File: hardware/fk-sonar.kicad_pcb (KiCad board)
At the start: 2 copper layers, 34.5 x 70.4 mm, 81 parts, among them J1 CONN_01x03, J10 CONN_01x02, J2 CONN_02x05_SWD, J3 RF-SMA-EDGE, J4 MICRO-USB, J5 S2B-PH-SM4-TB, J6 CONN_01x04, J7 S2B-PH-SM4-TB, J8 CONN_01x03_SERIAL, J9 CONN_01x05, M1 MOUNT_HOLE, M3 MOUNT_HOLE, M4 MOUNT_HOLE, M6 MOUNT_HOLE, Q1 2N7002LT1G, SW1 SPNO, U1 ATSAMD21G18A-AU, U2 RFM95W, U3 BQ24074RGTT, U4 S25FL116K0XMFI041, U5 MAX1704XX, U6 MCP1700T-3302E/MB, U7 SK6812, U8 TPS2051B, Y1 FC-135

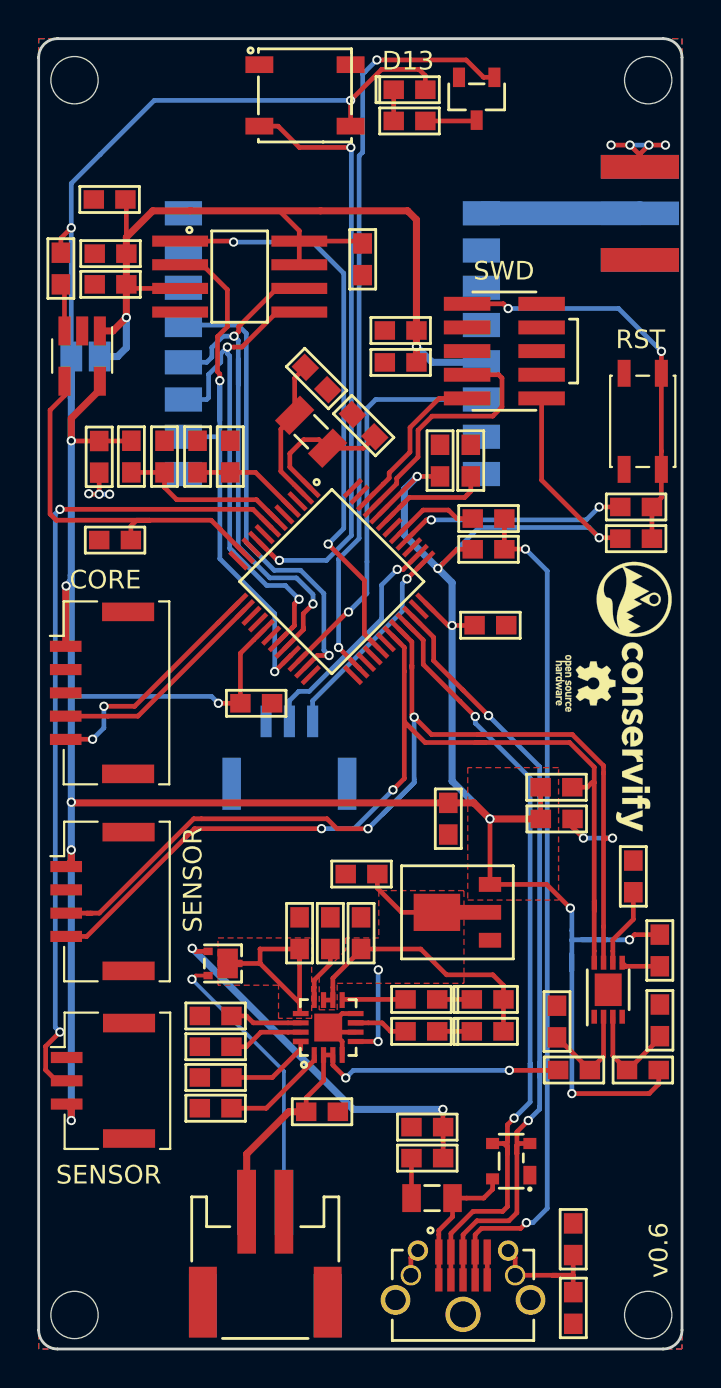
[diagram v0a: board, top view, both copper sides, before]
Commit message: Switch to 2.7mm mounting holes.
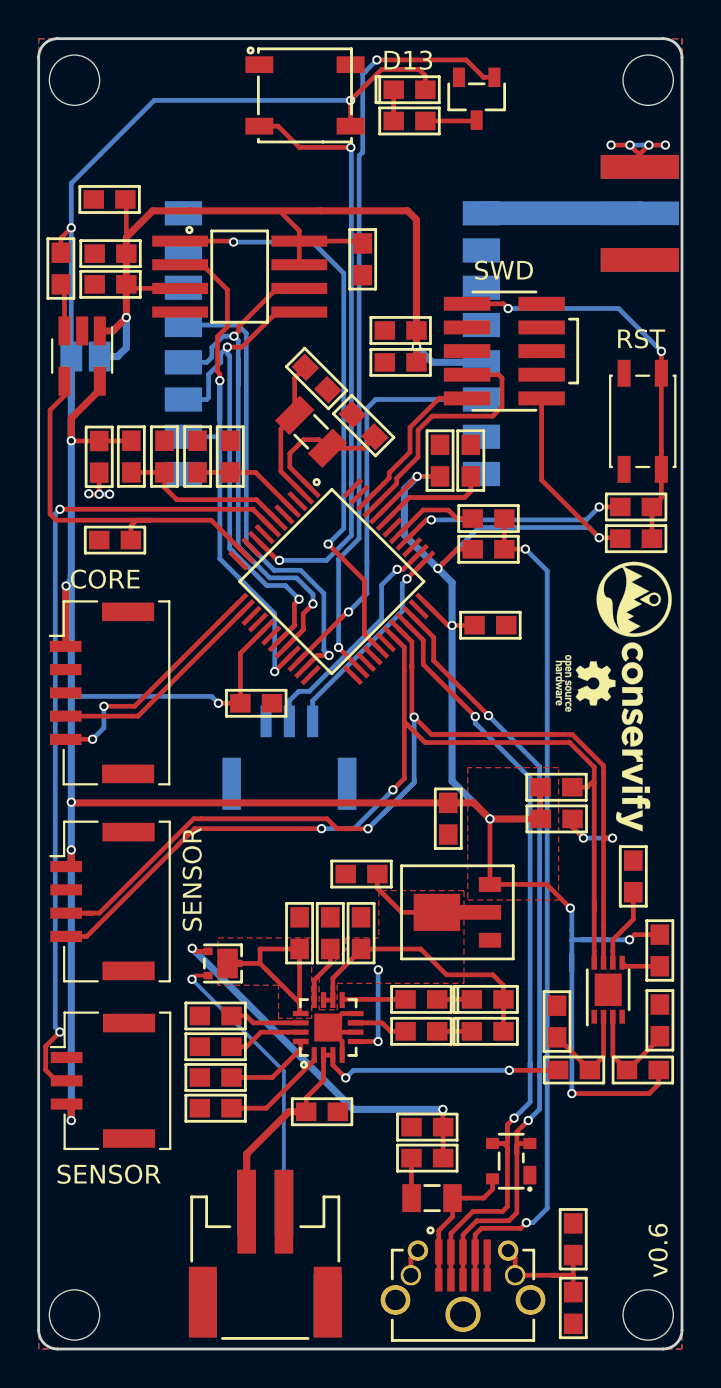
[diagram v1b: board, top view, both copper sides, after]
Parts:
- M1, M3, M4, M6: footprint conservify:HOLE_NPTH_2.54MM -> conservify:HOLE_NPTH_2.7MM
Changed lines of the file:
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@@
     )
-  )
-  (module conservify:HOLE_NPTH_2.54MM (layer F.Cu)
-    (at 154.9028 64.4608)
-    (fp_text reference M1 (at 0 -2.54) (layer F.SilkS) hide
-      (effects (font (size 1 1) (thickness 0.15)))
-    )
-    (fp_text value MOUNT_HOLE (at 0 2.54) (layer F.Fab)
-      (effects (font (size 1 1) (thickness 0.15)))
-    )
-    (pad "" np_thru_hole circle (at 0 0) (size 2.54 2.54) (drill 2.54) (layers *.Cu *.Mask F.SilkS))
-  )
-  (module conservify:HOLE_NPTH_2.54MM (layer F.Cu)
-    (at 124.1 130.7608)
-    (fp_text reference M3 (at 0 -2.54) (layer F.SilkS) hide
-      (effects (font (size 1 1) (thickness 0.15)))
-    )
-    (fp_text value MOUNT_HOLE (at 0 2.54) (layer F.Fab)
-      (effects (font (size 1 1) (thickness 0.15)))
-    )
-    (pad "" np_thru_hole circle (at 0 0) (size 2.54 2.54) (drill 2.54) (layers *.Cu *.Mask F.SilkS))
-  )
-  (module conservify:HOLE_NPTH_2.54MM (layer F.Cu)
-    (at 154.9028 130.7608)
-    (fp_text reference M4 (at 0 -2.54) (layer F.SilkS) hide
-      (effects (font (size 1 1) (thickness 0.15)))
-    )
-    (fp_text value MOUNT_HOLE (at 0 2.54) (layer F.Fab)
-      (effects (font (size 1 1) (thickness 0.15)))
-    )
-    (pad "" np_thru_hole circle (at 0 0) (size 2.54 2.54) (drill 2.54) (layers *.Cu *.Mask F.SilkS))
-  )
-  (module conservify:HOLE_NPTH_2.54MM (layer F.Cu)
-    (at 124.1 64.4608)
-    (fp_text reference M6 (at 0 -2.54) (layer F.SilkS) hide
-      (effects (font (size 1 1) (thickness 0.15)))
-    )
-    (fp_text value MOUNT_HOLE (at 0 2.54) (layer F.Fab)
-      (effects (font (size 1 1) (thickness 0.15)))
-    )
-    (pad "" np_thru_hole circle (at 0 0) (size 2.54 2.54) (drill 2.54) (layers *.Cu *.Mask F.SilkS))
   )
   (module conservify:RES-0603 (layer F.Cu)
@@
     (pad 2 smd rect (at 0.85 0) (size 1.1 1) (layers F.Cu F.Paste F.Mask)
       (net 86 /PERIPH_3V3))
+  )
+  (module conservify:HOLE_NPTH_2.7MM (layer F.Cu)
+    (at 154.9028 64.4608)
+    (fp_text reference M1 (at 0 -2.54) (layer F.SilkS) hide
+      (effects (font (size 1 1) (thickness 0.15)))
+    )
+    (fp_text value MOUNT_HOLE (at 0 2.54) (layer F.Fab)
+      (effects (font (size 1 1) (thickness 0.15)))
+    )
+    (pad "" np_thru_hole circle (at 0 0) (size 2.7 2.7) (drill 2.7) (layers *.Cu *.Mask F.SilkS))
+  )
+  (module conservify:HOLE_NPTH_2.7MM (layer F.Cu)
+    (at 124.1 130.7608)
+    (fp_text reference M3 (at 0 -2.54) (layer F.SilkS) hide
+      (effects (font (size 1 1) (thickness 0.15)))
+    )
+    (fp_text value MOUNT_HOLE (at 0 2.54) (layer F.Fab)
+      (effects (font (size 1 1) (thickness 0.15)))
+    )
+    (pad "" np_thru_hole circle (at 0 0) (size 2.7 2.7) (drill 2.7) (layers *.Cu *.Mask F.SilkS))
+  )
+  (module conservify:HOLE_NPTH_2.7MM (layer F.Cu)
+    (at 154.9028 130.7608)
+    (fp_text reference M4 (at 0 -2.54) (layer F.SilkS) hide
+      (effects (font (size 1 1) (thickness 0.15)))
+    )
+    (fp_text value MOUNT_HOLE (at 0 2.54) (layer F.Fab)
+      (effects (font (size 1 1) (thickness 0.15)))
+    )
+    (pad "" np_thru_hole circle (at 0 0) (size 2.7 2.7) (drill 2.7) (layers *.Cu *.Mask F.SilkS))
+  )
+  (module conservify:HOLE_NPTH_2.7MM (layer F.Cu)
+    (at 124.1 64.4608)
+    (fp_text reference M6 (at 0 -2.54) (layer F.SilkS) hide
+      (effects (font (size 1 1) (thickness 0.15)))
+    )
+    (fp_text value MOUNT_HOLE (at 0 2.54) (layer F.Fab)
+      (effects (font (size 1 1) (thickness 0.15)))
+    )
+    (pad "" np_thru_hole circle (at 0 0) (size 2.7 2.7) (drill 2.7) (layers *.Cu *.Mask F.SilkS))
   )
   (gr_text DEBUG (at 135.8392 105.5878 180) (layer B.SilkS)
@@
     (connect_pads (clearance 0.2032))
     (min_thickness 0.2032)
-    (fill yes (arc_segments 32) (thermal_gap 0.254) (thermal_bridge_width 0.254))
+    (fill (arc_segments 32) (thermal_gap 0.254) (thermal_bridge_width 0.254))
     (polygon
       (pts
@@
     (connect_pads (clearance 0.2032))
     (min_thickness 0.2032)
-    (fill yes (arc_segments 16) (thermal_gap 0.254) (thermal_bridge_width 0.254))
+    (fill (arc_segments 16) (thermal_gap 0.254) (thermal_bridge_width 0.254))
     (polygon
       (pts
@@
     (connect_pads (clearance 0.2032))
     (min_thickness 0.2032)
-    (fill yes (arc_segments 32) (thermal_gap 0.254) (thermal_bridge_width 0.254))
+    (fill (arc_segments 32) (thermal_gap 0.254) (thermal_bridge_width 0.254))
     (polygon
       (pts
@@
     (connect_pads (clearance 0.2032))
     (min_thickness 0.2032)
-    (fill yes (arc_segments 32) (thermal_gap 0.254) (thermal_bridge_width 0.254))
+    (fill (arc_segments 32) (thermal_gap 0.254) (thermal_bridge_width 0.254))
     (polygon
       (pts
@@
     (connect_pads (clearance 0.2032))
     (min_thickness 0.2032)
-    (fill yes (arc_segments 32) (thermal_gap 0.254) (thermal_bridge_width 0.254))
+    (fill (arc_segments 32) (thermal_gap 0.254) (thermal_bridge_width 0.254))
     (polygon
       (pts

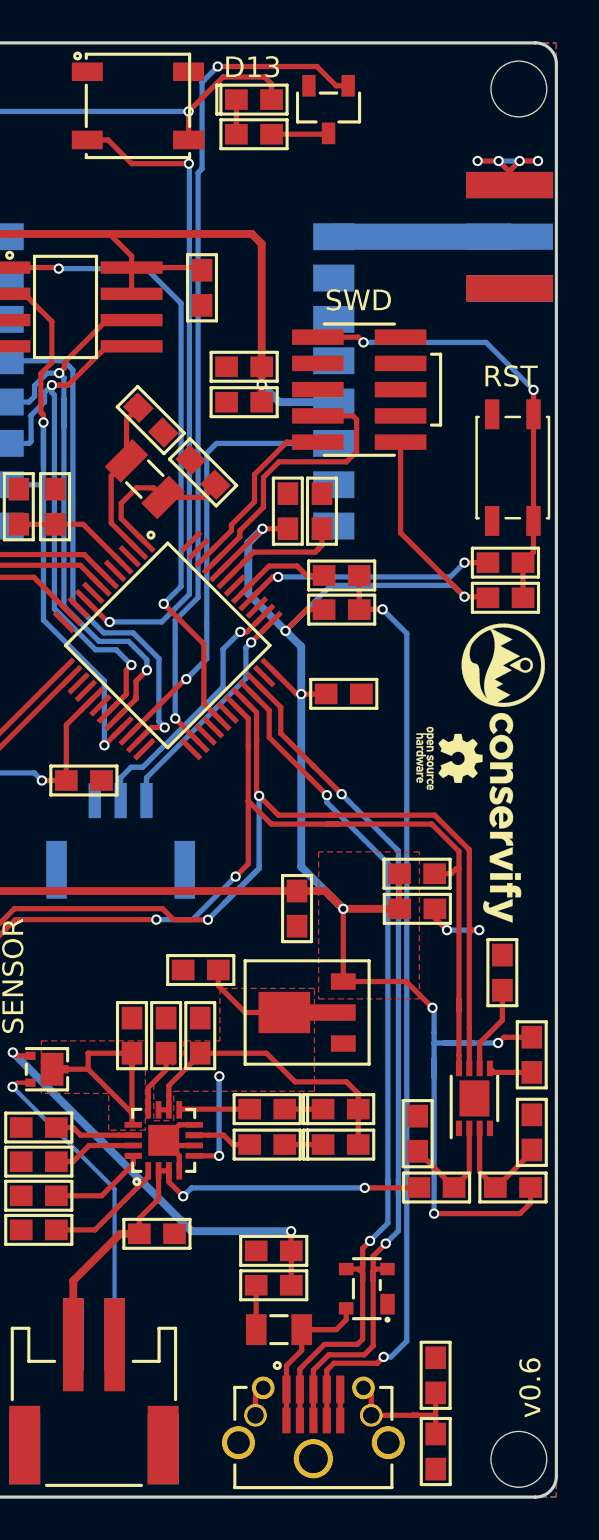
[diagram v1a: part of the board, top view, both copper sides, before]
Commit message: Deleted charging, LoRa, fuel gauge, swapped out connectors and peripheral switch
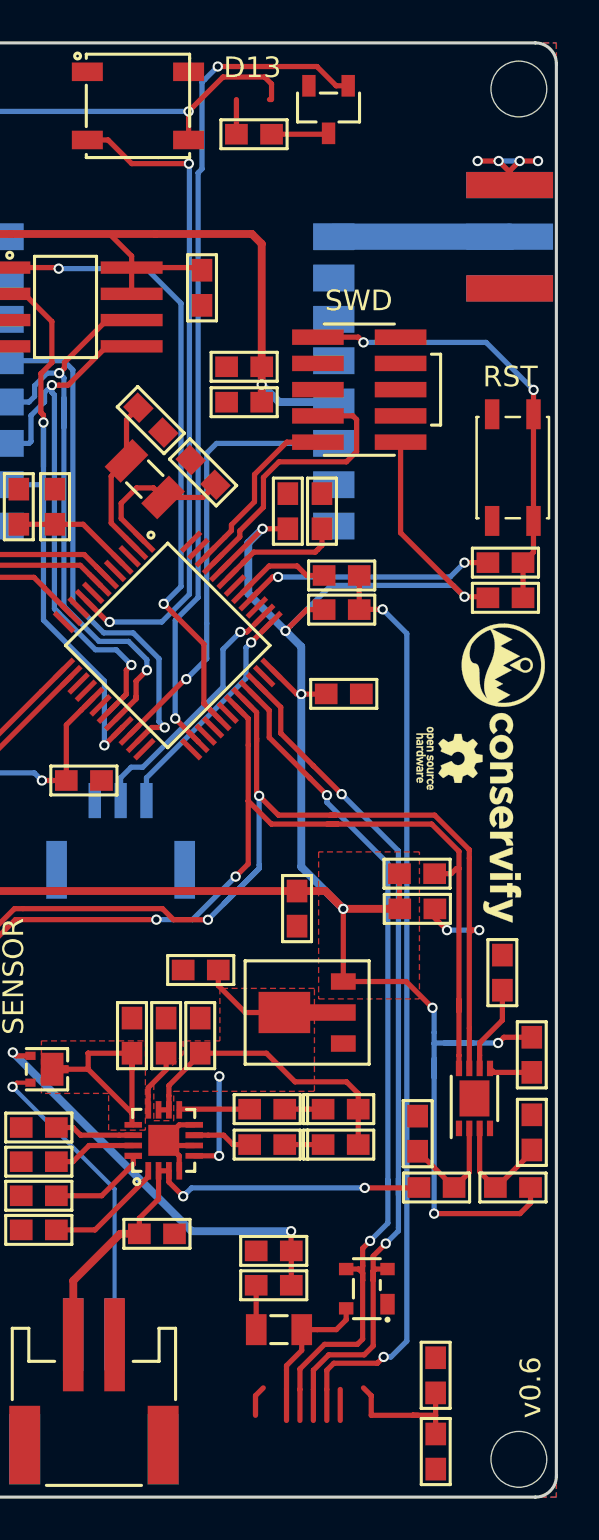
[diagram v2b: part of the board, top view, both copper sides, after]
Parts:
- removed D1: Orange, conservify:LED-0603
- removed J4: MICRO-USB, conservify:MICRO-USB
